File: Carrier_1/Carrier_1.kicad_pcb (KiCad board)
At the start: 2 copper layers, 30 x 22 mm, 2 parts, among them J1 Chubut_2 connector, U1 LGAD_1_pad

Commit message: First version
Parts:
- added C1: 1n, Capacitor_SMD:C_1206_3216Metric_Pad1.33x1.80mm_HandSolder, F.Cu at (105.9, 99.7)
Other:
- board size 30 x 22 mm -> 31.5 x 20.8 mm
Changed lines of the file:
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@@
     (property "Sheetname" "")
     (attr smd)
-    (fp_text reference "J1" (at 0 -0.5 unlocked) (layer "F.SilkS")
+    (fp_text reference "J1" (at 0 -0.5 unlocked) (layer "F.SilkS") hide
       (effects (font (size 1 1) (thickness 0.15)))
     )
@@
     )
   )
+  (footprint "Capacitor_SMD:C_1206_3216Metric_Pad1.33x1.80mm_HandSolder" (layer "F.Cu")
+    (at 105.93 99.74 180)
+    (descr "Capacitor SMD 1206 (3216 Metric), square (rectangular) end terminal, IPC_7351 nominal with elongated pad for handsoldering. (Body size source: IPC-SM-782 page 76, https://www.pcb-3d.com/wordpress/wp-content/uploads/ipc-sm-782a_amendment_1_and_2.pdf), generated with kicad-footprint-generator")
+    (tags "capacitor handsolder")
+    (property "Digikey" "https://www.digikey.ch/short/jfv8hn77")
+    (property "Manufacturer" "KYOCERA AVX")
+    (property "Manufacturer number" "1206GC102KAT1A")
+    (property "Sheetfile" "Carrier_1.kicad_sch")
+    (property "Sheetname" "")
+    (attr smd)
+    (fp_text reference "C1" (at 0 -1.85) (layer "F.SilkS")
+      (effects (font (size 1 1) (thickness 0.15)))
+    )
+    (fp_text value "1n" (at 0 1.85) (layer "F.Fab")
+      (effects (font (size 1 1) (thickness 0.15)))
+    )
+    (fp_text user "${REFERENCE}" (at 0 0) (layer "F.Fab")
+      (effects (font (size 0.8 0.8) (thickness 0.12)))
+    )
+    (fp_line (start -0.711252 -0.91) (end 0.711252 -0.91) (layer "F.SilkS") (width 0.12))
+    (fp_line (start -0.711252 0.91) (end 0.711252 0.91) (layer "F.SilkS") (width 0.12))
+    (fp_line (start -2.48 1.15) (end -2.48 -1.15) (layer "F.CrtYd") (width 0.05))
+    (fp_line (start 2.48 -1.15) (end 2.48 1.15) (layer "F.CrtYd") (width 0.05))
+    (fp_line (start -2.48 -1.15) (end 2.48 -1.15) (layer "F.CrtYd") (width 0.05))
+    (fp_line (start 2.48 1.15) (end -2.48 1.15) (layer "F.CrtYd") (width 0.05))
+    (fp_line (start 1.6 0.8) (end -1.6 0.8) (layer "F.Fab") (width 0.1))
+    (fp_line (start 1.6 -0.8) (end 1.6 0.8) (layer "F.Fab") (width 0.1))
+    (fp_line (start -1.6 -0.8) (end 1.6 -0.8) (layer "F.Fab") (width 0.1))
+    (fp_line (start -1.6 0.8) (end -1.6 -0.8) (layer "F.Fab") (width 0.1))
+    (pad "1" smd roundrect (at -1.5625 0 180) (size 1.325 1.8) (layers "F.Cu" "F.Paste" "F.Mask") (roundrect_rratio 0.188679)
+      (net 3 "Net-(J1-Pad5)") (pintype "passive"))
+    (pad "2" smd roundrect (at 1.5625 0 180) (size 1.325 1.8) (layers "F.Cu" "F.Paste" "F.Mask") (roundrect_rratio 0.188679)
+      (net 1 "GND") (pintype "passive"))
+    (model "${KICAD6_3DMODEL_DIR}/Capacitor_SMD.3dshapes/C_1206_3216Metric.wrl"
+      (offset (xyz 0 0 0))
+      (scale (xyz 1 1 1))
+      (rotate (xyz 0 0 0))
+    )
+  )
   (footprint "chubut:LGAD" (layer "F.Cu")
     (at 110 92)
@@
     (property "Sheetname" "")
     (attr smd)
-    (fp_text reference "U1" (at 25 -1 unlocked) (layer "F.SilkS")
+    (fp_text reference "U1" (at 25 -1 unlocked) (layer "F.SilkS") hide
       (effects (font (size 1 1) (thickness 0.15)))
     )
@@
     (pad "1" smd rect (at 0 0) (size 2 2) (layers "F.Cu" "F.Paste" "F.Mask")
       (net 2 "Net-(J1-Pad3)") (pintype "unspecified"))
+    (pad "2" smd rect (at 0 -4.5) (size 2 5) (layers "F.Cu" "F.Paste" "F.Mask")
+      (net 1 "GND") (pintype "unspecified"))
     (pad "2" smd rect (at 0 4.5) (size 2 5) (layers "F.Cu" "F.Paste" "F.Mask")
       (net 1 "GND") (pintype "unspecified"))
-    (pad "2" smd rect (at 0 -4.5) (size 2 5) (layers "F.Cu" "F.Paste" "F.Mask")
-      (net 1 "GND") (pintype "unspecified"))
     (pad "3" smd roundrect (at 2.75 0) (size 1.5 20) (layers "F.Cu" "F.Paste" "F.Mask") (roundrect_rratio 0.3333333333)
+      (net 3 "Net-(J1-Pad5)") (pintype "unspecified"))
+    (pad "3" smd roundrect (at 12 -9 90) (size 2 20) (layers "F.Cu" "F.Paste" "F.Mask") (roundrect_rratio 0.25)
       (net 3 "Net-(J1-Pad5)") (pintype "unspecified"))
     (pad "3" smd roundrect (at 12 9 90) (size 2 20) (layers "F.Cu" "F.Paste" "F.Mask") (roundrect_rratio 0.25)
       (net 3 "Net-(J1-Pad5)") (pintype "unspecified"))
     (pad "3" smd roundrect (at 13.25 0) (size 17.5 20) (layers "F.Cu" "F.Paste" "F.Mask") (roundrect_rratio 0.02857142857)
-      (net 3 "Net-(J1-Pad5)") (pintype "unspecified"))
-    (pad "3" smd roundrect (at 12 -9 90) (size 2 20) (layers "F.Cu" "F.Paste" "F.Mask") (roundrect_rratio 0.25)
       (net 3 "Net-(J1-Pad5)") (pintype "unspecified"))
     (zone (net 0) (net_name "") (layers "F.Adhes" "F.Paste" "F.SilkS" "F.Mask" "F.CrtYd") (hatch edge 0.508)
@@
       )
     )
+    (model "/home/alf/cernbox/projects/LGAD_stability/Chubut_2/libs/3D/very_big_LGAD.step"
+      (offset (xyz 12 0 0))
+      (scale (xyz 1 1 1))
+      (rotate (xyz 0 0 0))
+    )
   )
-  (gr_line (start 133 81) (end 103 81) (layer "Edge.Cuts") (width 0.1))
-  (gr_line (start 103 81) (end 103 103) (layer "Edge.Cuts") (width 0.1))
-  (gr_line (start 103 103) (end 133 103) (layer "Edge.Cuts") (width 0.1))
-  (gr_line (start 133 103) (end 133 81) (layer "Edge.Cuts") (width 0.1))
+  (gr_rect (start 103 81.6) (end 134.5 102.4) (layer "Edge.Cuts") (width 0.1) (fill none))
   (segment (start 109 94) (end 110 95) (width 0.25) (layer "F.Cu") (net 1))
   (segment (start 110 95) (end 110 96.5) (width 0.25) (layer "F.Cu") (net 1))
@@
     (polygon
       (pts
-        (xy 133 103)
-        (xy 103 103)
-        (xy 103 81)
-        (xy 133 81)
+        (xy 140.5 78)
+        (xy 141 106.5)
+        (xy 96 106.5)
+        (xy 93 76.5)
       )
     )

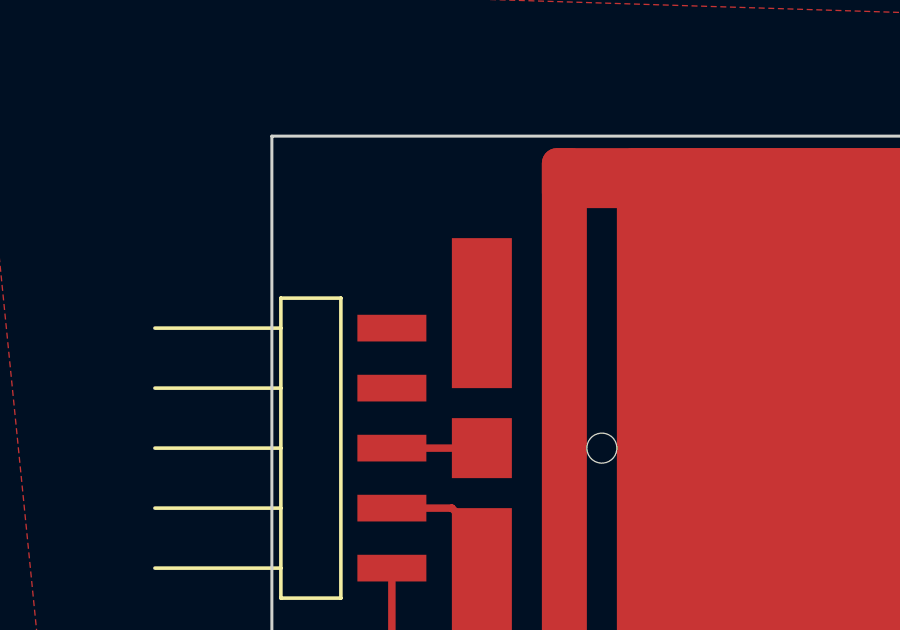
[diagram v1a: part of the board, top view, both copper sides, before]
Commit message: Updated the carrier to be compatible with 2 pad devices
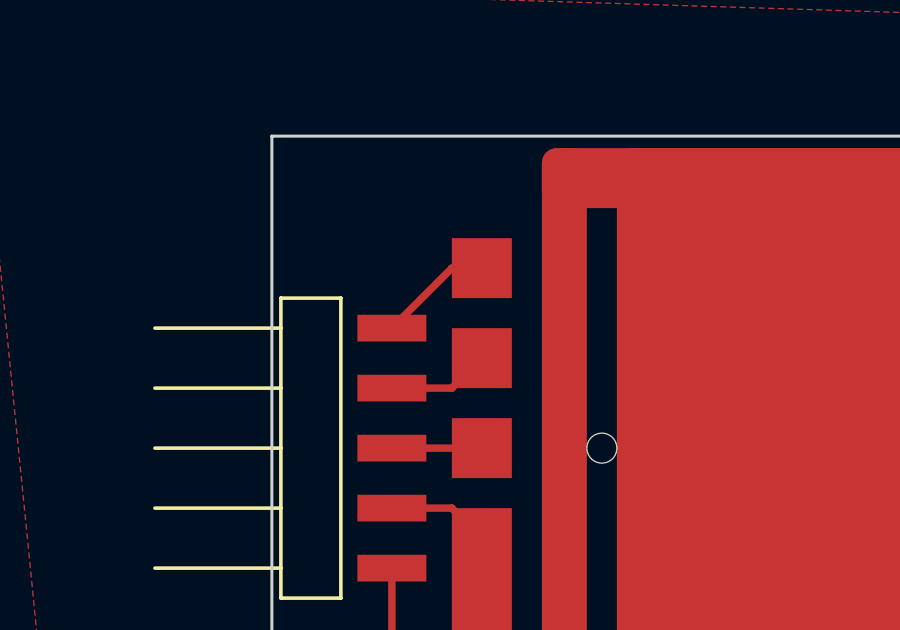
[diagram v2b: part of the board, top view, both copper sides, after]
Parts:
- U1: value LGAD_1_pad -> LGAD_2_pad
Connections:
- C1 pad 1: Net-(J1-Pad5) -> Net-(C1-Pad1)
- J1 pad 1: GND -> Net-(J1-Pad1)
- J1 pad 5: Net-(J1-Pad5) -> Net-(C1-Pad1)
- U1 pad 1: Net-(J1-Pad3) -> Net-(C1-Pad1)
- U1 pad 3: Net-(J1-Pad5) -> Net-(J1-Pad3)
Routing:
- net Net-(J1-Pad5): track 19.4 -> 0.00 mm
- net Net-(C1-Pad1): track 0.00 -> 19.4 mm
- net Net-(J1-Pad1): track 0.00 -> 3.83 mm
- net GND: track 4.91 -> 8.33 mm
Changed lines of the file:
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@@
   (net 1 "GND")
   (net 2 "Net-(J1-Pad3)")
-  (net 3 "Net-(J1-Pad5)")
+  (net 3 "Net-(C1-Pad1)")
+  (net 4 "Net-(J1-Pad1)")
+  (footprint "chubut:LGAD" (layer "F.Cu")
+    (at 110 92)
+    (property "Sheetfile" "Carrier_1.kicad_sch")
+    (property "Sheetname" "")
+    (attr smd)
+    (fp_text reference "U1" (at 25 -1 unlocked) (layer "F.SilkS") hide
+      (effects (font (size 1 1) (thickness 0.15)))
+    )
+    (fp_text value "LGAD_2_pad" (at 25 0.5 unlocked) (layer "F.Fab")
+      (effects (font (size 1 1) (thickness 0.15)))
+    )
+    (fp_text user "${REFERENCE}" (at 25 2 unlocked) (layer "F.Fab")
+      (effects (font (size 1 1) (thickness 0.15)))
+    )
+    (pad "" np_thru_hole circle (at 4 0) (size 1 1) (drill 1) (layers F&B.Cu))
+    (pad "1" smd roundrect (at 2.75 0) (size 1.5 20) (layers "F.Cu" "F.Paste" "F.Mask") (roundrect_rratio 0.3333333333)
+      (net 3 "Net-(C1-Pad1)") (pintype "unspecified"))
+    (pad "1" smd roundrect (at 13.25 0) (size 17.5 20) (layers "F.Cu" "F.Paste" "F.Mask") (roundrect_rratio 0.02857142857)
+      (net 3 "Net-(C1-Pad1)") (pintype "unspecified"))
+    (pad "1" smd roundrect (at 12 -9 90) (size 2 20) (layers "F.Cu" "F.Paste" "F.Mask") (roundrect_rratio 0.25)
+      (net 3 "Net-(C1-Pad1)") (pintype "unspecified"))
+    (pad "1" smd roundrect (at 12 9 90) (size 2 20) (layers "F.Cu" "F.Paste" "F.Mask") (roundrect_rratio 0.25)
+      (net 3 "Net-(C1-Pad1)") (pintype "unspecified"))
+    (pad "2" smd rect (at 0 -3) (size 2 2) (layers "F.Cu" "F.Paste" "F.Mask")
+      (net 1 "GND") (pintype "unspecified"))
+    (pad "2" smd rect (at 0 4.5) (size 2 5) (layers "F.Cu" "F.Paste" "F.Mask")
+      (net 1 "GND") (pintype "unspecified"))
+    (pad "3" smd rect (at 0 0) (size 2 2) (layers "F.Cu" "F.Paste" "F.Mask")
+      (net 2 "Net-(J1-Pad3)") (pintype "unspecified"))
+    (pad "4" smd rect (at 0 -6) (size 2 2) (layers "F.Cu" "F.Paste" "F.Mask")
+      (net 4 "Net-(J1-Pad1)") (pintype "unspecified"))
+    (zone (net 0) (net_name "") (layers "F.Adhes" "F.Paste" "F.SilkS" "F.Mask" "F.CrtYd") (hatch edge 0.508)
+      (connect_pads (clearance 0))
+      (min_thickness 0.254)
+      (keepout (tracks not_allowed) (vias not_allowed) (pads not_allowed ) (copperpour not_allowed) (footprints not_allowed))
+      (fill (thermal_gap 0.508) (thermal_bridge_width 0.508))
+      (polygon
+        (pts
+          (xy 133 103)
+          (xy 109 103)
+          (xy 109 81)
+          (xy 133 81)
+        )
+      )
+    )
+    (model "/home/alf/cernbox/projects/LGAD_stability/Chubut_2/libs/3D/very_big_LGAD.step"
+      (offset (xyz 12 0 0))
+      (scale (xyz 1 1 1))
+      (rotate (xyz 0 0 0))
+    )
+  )
   (footprint "chubut:M22-5330505" (layer "F.Cu")
     (at 107 83)
@@
     (fp_line (start 1.5 3.5) (end 1.5 14.5) (layer "F.CrtYd") (width 0.05))
     (pad "1" smd rect (at 0 5) (size 2.3 0.89) (layers "F.Cu" "F.Paste" "F.Mask")
-      (net 1 "GND") (pinfunction "Pin_1") (pintype "passive"))
+      (net 4 "Net-(J1-Pad1)") (pinfunction "Pin_1") (pintype "passive"))
     (pad "2" smd rect (at 0 7) (size 2.3 0.89) (layers "F.Cu" "F.Paste" "F.Mask")
       (net 1 "GND") (pinfunction "Pin_2") (pintype "passive"))
@@
       (net 1 "GND") (pinfunction "Pin_4") (pintype "passive"))
     (pad "5" smd rect (at 0 13) (size 2.3 0.89) (layers "F.Cu" "F.Paste" "F.Mask")
-      (net 3 "Net-(J1-Pad5)") (pinfunction "Pin_5") (pintype "passive"))
+      (net 3 "Net-(C1-Pad1)") (pinfunction "Pin_5") (pintype "passive"))
     (model "/home/alf/cernbox/projects/LGAD_stability/Chubut_2/libs/3D/M22-5330505.STEP"
       (offset (xyz 3.2 -8.84 -3.5))
@@
     (fp_line (start -1.6 0.8) (end -1.6 -0.8) (layer "F.Fab") (width 0.1))
     (pad "1" smd roundrect (at -1.5625 0 180) (size 1.325 1.8) (layers "F.Cu" "F.Paste" "F.Mask") (roundrect_rratio 0.188679)
-      (net 3 "Net-(J1-Pad5)") (pintype "passive"))
+      (net 3 "Net-(C1-Pad1)") (pintype "passive"))
     (pad "2" smd roundrect (at 1.5625 0 180) (size 1.325 1.8) (layers "F.Cu" "F.Paste" "F.Mask") (roundrect_rratio 0.188679)
       (net 1 "GND") (pintype "passive"))
@@
     )
   )
-  (footprint "chubut:LGAD" (layer "F.Cu")
-    (at 110 92)
-    (property "Sheetfile" "Carrier_1.kicad_sch")
-    (property "Sheetname" "")
-    (attr smd)
-    (fp_text reference "U1" (at 25 -1 unlocked) (layer "F.SilkS") hide
-      (effects (font (size 1 1) (thickness 0.15)))
-    )
-    (fp_text value "LGAD_1_pad" (at 25 0.5 unlocked) (layer "F.Fab")
-      (effects (font (size 1 1) (thickness 0.15)))
-    )
-    (fp_text user "${REFERENCE}" (at 25 2 unlocked) (layer "F.Fab")
-      (effects (font (size 1 1) (thickness 0.15)))
-    )
-    (pad "" np_thru_hole circle (at 4 0) (size 1 1) (drill 1) (layers F&B.Cu))
-    (pad "1" smd rect (at 0 0) (size 2 2) (layers "F.Cu" "F.Paste" "F.Mask")
-      (net 2 "Net-(J1-Pad3)") (pintype "unspecified"))
-    (pad "2" smd rect (at 0 -4.5) (size 2 5) (layers "F.Cu" "F.Paste" "F.Mask")
-      (net 1 "GND") (pintype "unspecified"))
-    (pad "2" smd rect (at 0 4.5) (size 2 5) (layers "F.Cu" "F.Paste" "F.Mask")
-      (net 1 "GND") (pintype "unspecified"))
-    (pad "3" smd roundrect (at 2.75 0) (size 1.5 20) (layers "F.Cu" "F.Paste" "F.Mask") (roundrect_rratio 0.3333333333)
-      (net 3 "Net-(J1-Pad5)") (pintype "unspecified"))
-    (pad "3" smd roundrect (at 12 -9 90) (size 2 20) (layers "F.Cu" "F.Paste" "F.Mask") (roundrect_rratio 0.25)
-      (net 3 "Net-(J1-Pad5)") (pintype "unspecified"))
-    (pad "3" smd roundrect (at 12 9 90) (size 2 20) (layers "F.Cu" "F.Paste" "F.Mask") (roundrect_rratio 0.25)
-      (net 3 "Net-(J1-Pad5)") (pintype "unspecified"))
-    (pad "3" smd roundrect (at 13.25 0) (size 17.5 20) (layers "F.Cu" "F.Paste" "F.Mask") (roundrect_rratio 0.02857142857)
-      (net 3 "Net-(J1-Pad5)") (pintype "unspecified"))
-    (zone (net 0) (net_name "") (layers "F.Adhes" "F.Paste" "F.SilkS" "F.Mask" "F.CrtYd") (hatch edge 0.508)
-      (connect_pads (clearance 0))
-      (min_thickness 0.254)
-      (keepout (tracks not_allowed) (vias not_allowed) (pads not_allowed ) (copperpour not_allowed) (footprints not_allowed))
-      (fill (thermal_gap 0.508) (thermal_bridge_width 0.508))
-      (polygon
-        (pts
-          (xy 133 103)
-          (xy 109 103)
-          (xy 109 81)
-          (xy 133 81)
-        )
-      )
-    )
-    (model "/home/alf/cernbox/projects/LGAD_stability/Chubut_2/libs/3D/very_big_LGAD.step"
-      (offset (xyz 12 0 0))
-      (scale (xyz 1 1 1))
-      (rotate (xyz 0 0 0))
-    )
-  )
   (gr_rect (start 103 81.6) (end 134.5 102.4) (layer "Edge.Cuts") (width 0.1) (fill none))
+  (segment (start 107 90) (end 109 90) (width 0.25) (layer "F.Cu") (net 1))
   (segment (start 109 94) (end 110 95) (width 0.25) (layer "F.Cu") (net 1))
   (segment (start 110 95) (end 110 96.5) (width 0.25) (layer "F.Cu") (net 1))
   (segment (start 107 94) (end 109 94) (width 0.25) (layer "F.Cu") (net 1))
+  (segment (start 109 90) (end 110 89) (width 0.25) (layer "F.Cu") (net 1))
   (segment (start 110 92) (end 107 92) (width 0.25) (layer "F.Cu") (net 2))
   (segment (start 107 100) (end 108 101) (width 0.25) (layer "F.Cu") (net 3))
   (segment (start 107 96) (end 107 100) (width 0.25) (layer "F.Cu") (net 3))
   (segment (start 108 101) (end 122 101) (width 0.25) (layer "F.Cu") (net 3))
+  (segment (start 109 86) (end 110 86) (width 0.25) (layer "F.Cu") (net 4))
+  (segment (start 107 88) (end 109 86) (width 0.25) (layer "F.Cu") (net 4))
   (zone (net 1) (net_name "GND") (layer "F.Cu") (hatch edge 0.508)
     (connect_pads (clearance 0.508))
